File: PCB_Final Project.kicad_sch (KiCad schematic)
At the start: 23 parts, among them J2 Conn_01x02_Pin, J4 Conn_01x02_Socket, K1 SANYOU_SRD_Form_C, Q1 BC547, U1 WeMos_D1_mini, U3 LM393

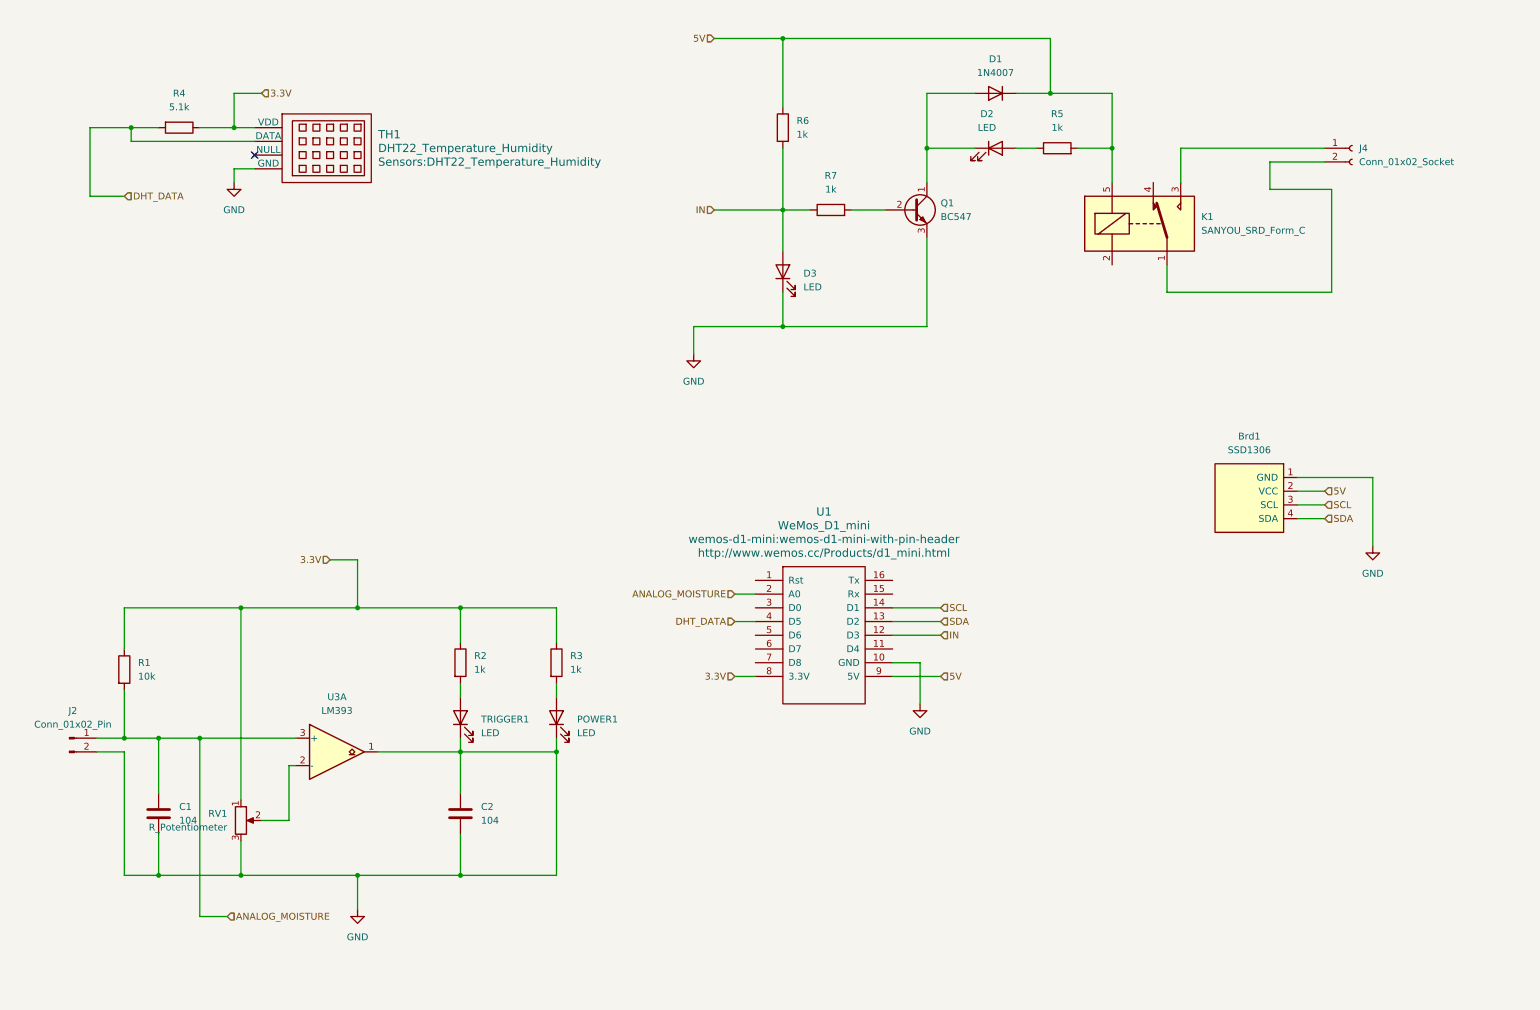
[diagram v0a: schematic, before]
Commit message: update schematic
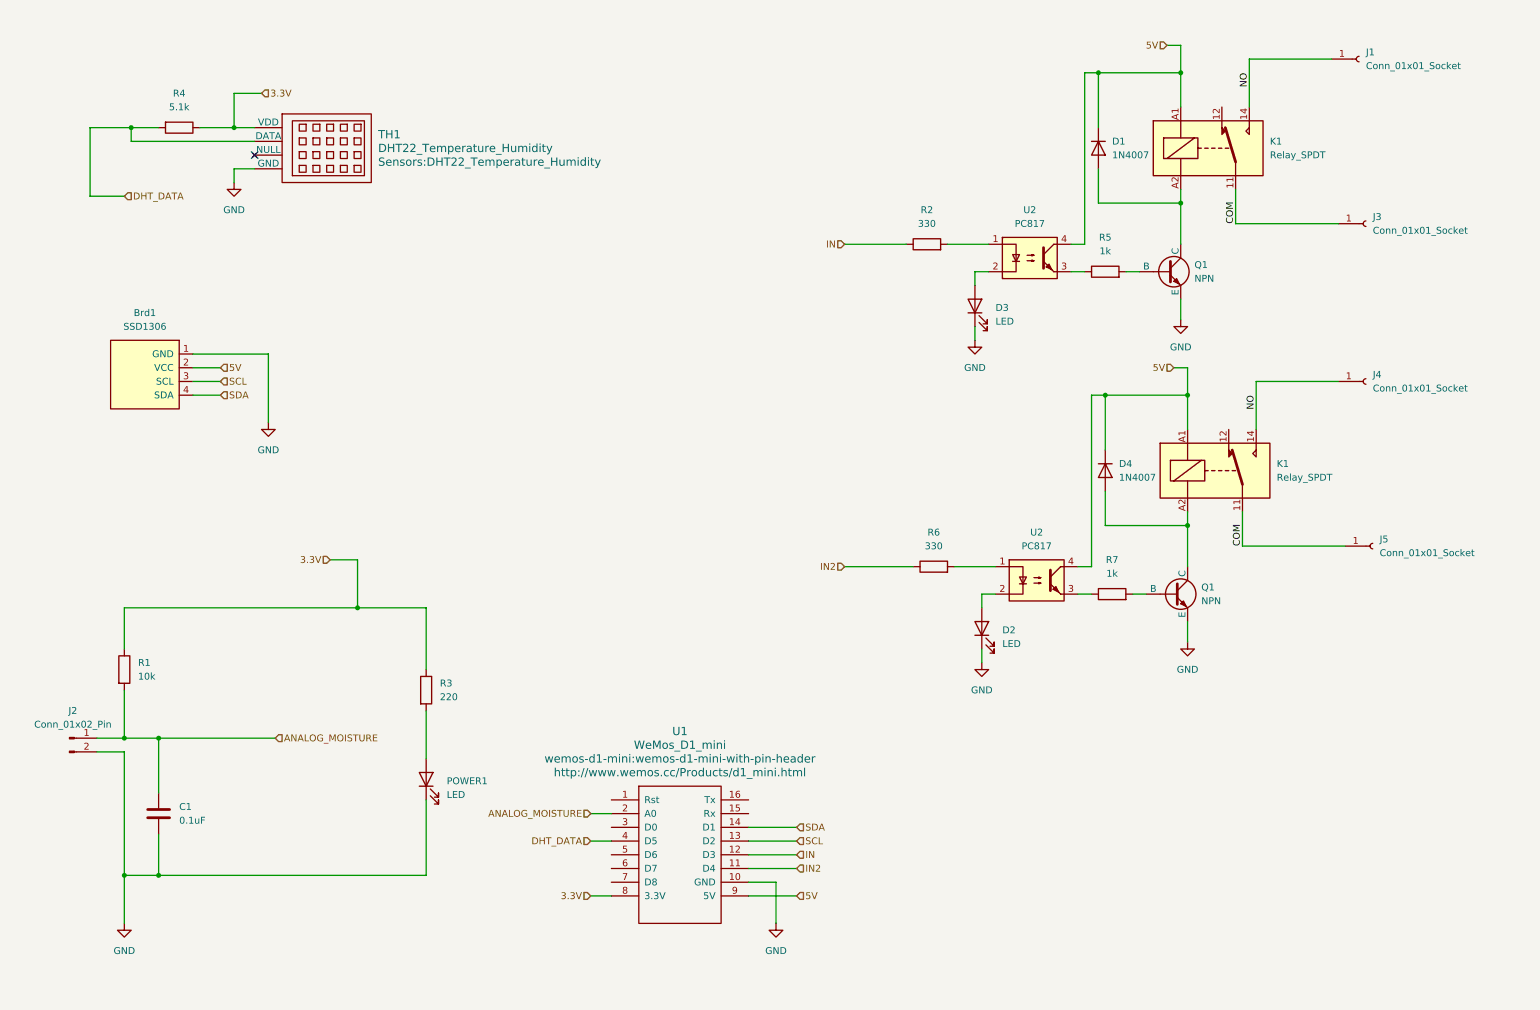
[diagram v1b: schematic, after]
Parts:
- removed C2: 104, Capacitor_SMD:C_0805_2012Metric, symbol Device:C
- removed J4: Conn_01x02_Socket, Connector_PinHeader_2.54mm:PinHeader_1x02_P2.54mm_Vertical, symbol Connector:Conn_01x02_Socket
- removed K1: SANYOU_SRD_Form_C, Relay_SMD:Relay_DPDT_Omron_G6K-2F, symbol Relay:SANYOU_SRD_Form_C
- removed Q1: BC547, Package_TO_SOT_THT:TO-92_Inline, symbol Transistor_BJT:BC547
- removed RV1: R_Potentiometer, Potentiometer_THT:Potentiometer_Piher_PT-15-V02_Vertical_Hole, symbol Device:R_Potentiometer
- removed TRIGGER1: LED, LED_SMD:LED_0805_2012Metric, symbol Device:LED
- removed U3: LM393, Package_DIP:DIP-8_W7.62mm, symbol Comparator:LM393
- added D4: 1N4007, Diode_THT:D_DO-41_SOD81_P10.16mm_Horizontal, symbol Diode:1N4007
- added J1, J3, J4, J5: Conn_01x01_Socket, Connector_PinHeader_2.54mm:PinHeader_1x01_P2.54mm_Vertical, symbol Connector:Conn_01x01_Socket
- added K1 (x2): Relay_SPDT, Relay_THT:Relay_SPDT_Finder_36.11, symbol Relay:Relay_SPDT
- added Q1 (x2): NPN, Package_TO_SOT_SMD:TSOT-23, symbol Simulation_SPICE:NPN
- added U2 (x2): PC817, Package_DIP:DIP-4_W7.62mm_SMDSocket_SmallPads, symbol Isolator:PC817
- C1: value 104 -> 0.1uF
- R2, R6: value 1k -> 330
- R3: value 1k -> 220
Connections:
- net 3.3V: no longer R2.1
- net 5V: now also D4.1 (K), K1.A1, K1.A1, U2.4, U2.4; no longer R5.2, R6.1
- net GND: now also D2.1 (K), Q1.3 (E), Q1.3 (E)
- net IN: now also R2.1; no longer D3.2 (A), R6.2, R7.1
- net SCL: now also U1.13 (D2); no longer U1.14 (D1)
- net SDA: now also U1.14 (D1); no longer U1.13 (D2)
- net at R7.2: now also Q1.2 (B)
- net at R2.2: now also U2.1
- net at D1.2 (A): now also K1.A2, Q1.1 (C); no longer D2.1 (K)
- net at R5.1: now also U2.3; no longer D2.2 (A)
- net IN2: now reaches U1.11 (D4)
- net IN2: now also R6.1
- new net: D4.2 (A), K1.A2, Q1.1 (C)
- new net: R6.2, U2.1
- new net: Q1.2 (B), R5.2
- new net: D3.2 (A), U2.2
- new net: R7.1, U2.3
- new net: D2.2 (A), U2.2
- new net COM: J3.1 (Pin_1), J5.1 (Pin_1), K1.11, K1.11
- new net NO: J1.1 (Pin_1), J4.1 (Pin_1), K1.14, K1.14
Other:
- moved on the sheet: Brd1, POWER1, R3, U1

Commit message: pcb done
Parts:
- removed J1, J3, J4, J5: Conn_01x01_Socket, Connector_PinHeader_2.54mm:PinHeader_1x01_P2.54mm_Vertical, symbol Connector:Conn_01x01_Socket
- added J1, J3: Conn_01x02_Socket, Connector_Wire:SolderWire-2.5sqmm_1x02_P8.8mm_D2.4mm_OD4.4mm, symbol Connector:Conn_01x02_Socket
- D1, D4: footprint Diode_THT:D_DO-41_SOD81_P10.16mm_Horizontal -> Diode_SMD:D_0805_2012Metric
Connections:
- net COM: now also J1.2 (Pin_2), J3.2 (Pin_2)
- net NO: now also J1.1 (Pin_1), J3.1 (Pin_1)
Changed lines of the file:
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@@
+    (stroke (width 0) (type default))
+  )
+  (wire (pts (xy 266.7 99.06) (xy 262.89 99.06))
+    (stroke (width 0) (type default))
+  )
+  (wire (pts (xy 262.89 99.06) (xy 262.89 113.03))
     (stroke (width 0) (type default))
   )
@@
     (stroke (width 0) (type default))
   )
-  (wire (pts (xy 241.3 113.03) (xy 260.35 113.03))
+  (wire (pts (xy 241.3 113.03) (xy 262.89 113.03))
     (stroke (width 0) (type default))
   )
@@
     (stroke (width 0) (type default))
   )
-  (wire (pts (xy 240.03 53.34) (xy 259.08 53.34))
+  (wire (pts (xy 240.03 53.34) (xy 261.62 53.34))
     (stroke (width 0) (type default))
   )
@@
     (stroke (width 0) (type default))
   )
-  (wire (pts (xy 242.57 22.86) (xy 257.81 22.86))
+  (wire (pts (xy 242.57 22.86) (xy 261.62 22.86))
+    (stroke (width 0) (type default))
+  )
+  (wire (pts (xy 261.62 38.1) (xy 264.16 38.1))
     (stroke (width 0) (type default))
   )
@@
     (stroke (width 0) (type default))
   )
-  (wire (pts (xy 243.84 82.55) (xy 259.08 82.55))
+  (wire (pts (xy 243.84 82.55) (xy 262.89 82.55))
     (stroke (width 0) (type default))
   )
@@
     (stroke (width 0) (type default))
   )
+  (wire (pts (xy 262.89 82.55) (xy 262.89 96.52))
+    (stroke (width 0) (type default))
+  )
   (wire (pts (xy 60.96 77.47) (xy 60.96 90.17))
     (stroke (width 0) (type default))
   )
+  (wire (pts (xy 264.16 40.64) (xy 261.62 40.64))
+    (stroke (width 0) (type default))
+  )
   (wire (pts (xy 40.64 148.59) (xy 40.64 158.75))
     (stroke (width 0) (type default))
@@
     (stroke (width 0) (type default))
   )
+  (wire (pts (xy 261.62 22.86) (xy 261.62 38.1))
+    (stroke (width 0) (type default))
+  )
   (wire (pts (xy 40.64 173.99) (xy 90.17 173.99))
     (stroke (width 0) (type default))
@@
   )
   (wire (pts (xy 243.84 91.44) (xy 243.84 82.55))
+    (stroke (width 0) (type default))
+  )
+  (wire (pts (xy 262.89 96.52) (xy 266.7 96.52))
+    (stroke (width 0) (type default))
+  )
+  (wire (pts (xy 261.62 40.64) (xy 261.62 53.34))
     (stroke (width 0) (type default))
   )
@@
       (effects (font (size 1.27 1.27)) (justify left))
     )
-    (property "Footprint" "Diode_THT:D_DO-41_SOD81_P10.16mm_Horizontal" (at 211.455 99.06 0)
+    (property "Footprint" "Diode_SMD:D_0805_2012Metric" (at 211.455 99.06 0)
       (effects (font (size 1.27 1.27)) hide)
     )
@@
         (path "/5c4b6275-3c5c-44a0-af63-482a4c493fbb"
           (reference "D4") (unit 1)
+        )
+      )
+    )
+  )
+  (symbol (lib_id "Connector:Conn_01x02_Socket") (at 271.78 96.52 0) (unit 1)
+    (in_bom yes) (on_board yes) (dnp no) (fields_autoplaced)
+    (property "Reference" "J3" (at 273.05 96.52 0)
+      (effects (font (size 1.27 1.27)) (justify left))
+    )
+    (property "Value" "Conn_01x02_Socket" (at 273.05 99.06 0)
+      (effects (font (size 1.27 1.27)) (justify left))
+    )
+    (property "Footprint" "Connector_Wire:SolderWire-2.5sqmm_1x02_P8.8mm_D2.4mm_OD4.4mm" (at 271.78 96.52 0)
+      (effects (font (size 1.27 1.27)) hide)
+    )
+    (property "Datasheet" "~" (at 271.78 96.52 0)
+      (effects (font (size 1.27 1.27)) hide)
+    )
+    (pin "1")
+    (pin "2")
+    (instances
+      (project "PCB_Final Project"
+        (path "/5c4b6275-3c5c-44a0-af63-482a4c493fbb"
+          (reference "J3") (unit 1)
         )
       )
@@
     )
   )
-  (symbol (lib_id "Connector:Conn_01x01_Socket") (at 264.16 82.55 0) (unit 1)
-    (in_bom yes) (on_board yes) (dnp no) (fields_autoplaced)
-    (property "Reference" "J4" (at 265.43 81.28 0)
-      (effects (font (size 1.27 1.27)) (justify left))
-    )
-    (property "Value" "Conn_01x01_Socket" (at 265.43 83.82 0)
-      (effects (font (size 1.27 1.27)) (justify left))
-    )
-    (property "Footprint" "Connector_PinHeader_2.54mm:PinHeader_1x01_P2.54mm_Vertical" (at 264.16 82.55 0)
-      (effects (font (size 1.27 1.27)) hide)
-    )
-    (property "Datasheet" "~" (at 264.16 82.55 0)
-      (effects (font (size 1.27 1.27)) hide)
-    )
-    (pin "1")
-    (instances
-      (project "PCB_Final Project"
-        (path "/5c4b6275-3c5c-44a0-af63-482a4c493fbb"
-          (reference "J4") (unit 1)
-        )
-      )
-    )
-  )
   (symbol (lib_id "Device:R") (at 34.29 135.89 0) (unit 1)
     (in_bom yes) (on_board yes) (dnp no) (fields_autoplaced)
@@
       (effects (font (size 1.27 1.27)) (justify left))
     )
-    (property "Footprint" "Diode_THT:D_DO-41_SOD81_P10.16mm_Horizontal" (at 210.185 39.37 0)
+    (property "Footprint" "Diode_SMD:D_0805_2012Metric" (at 210.185 39.37 0)
       (effects (font (size 1.27 1.27)) hide)
     )
@@
     )
   )
-  (symbol (lib_id "Connector:Conn_01x01_Socket") (at 264.16 53.34 0) (unit 1)
-    (in_bom yes) (on_board yes) (dnp no) (fields_autoplaced)
-    (property "Reference" "J3" (at 265.43 52.07 0)
-      (effects (font (size 1.27 1.27)) (justify left))
-    )
-    (property "Value" "Conn_01x01_Socket" (at 265.43 54.61 0)
-      (effects (font (size 1.27 1.27)) (justify left))
-    )
-    (property "Footprint" "Connector_PinHeader_2.54mm:PinHeader_1x01_P2.54mm_Vertical" (at 264.16 53.34 0)
-      (effects (font (size 1.27 1.27)) hide)
-    )
-    (property "Datasheet" "~" (at 264.16 53.34 0)
-      (effects (font (size 1.27 1.27)) hide)
-    )
-    (pin "1")
-    (instances
-      (project "PCB_Final Project"
-        (path "/5c4b6275-3c5c-44a0-af63-482a4c493fbb"
-          (reference "J3") (unit 1)
-        )
-      )
-    )
-  )
   (symbol (lib_id "Isolator:PC817") (at 203.2 119.38 0) (unit 1)
     (in_bom yes) (on_board yes) (dnp no) (fields_autoplaced)
@@
         (path "/5c4b6275-3c5c-44a0-af63-482a4c493fbb"
           (reference "D2") (unit 1)
+        )
+      )
+    )
+  )
+  (symbol (lib_id "Connector:Conn_01x02_Socket") (at 269.24 38.1 0) (unit 1)
+    (in_bom yes) (on_board yes) (dnp no) (fields_autoplaced)
+    (property "Reference" "J1" (at 270.51 38.1 0)
+      (effects (font (size 1.27 1.27)) (justify left))
+    )
+    (property "Value" "Conn_01x02_Socket" (at 270.51 40.64 0)
+      (effects (font (size 1.27 1.27)) (justify left))
+    )
+    (property "Footprint" "Connector_Wire:SolderWire-2.5sqmm_1x02_P8.8mm_D2.4mm_OD4.4mm" (at 269.24 38.1 0)
+      (effects (font (size 1.27 1.27)) hide)
+    )
+    (property "Datasheet" "~" (at 269.24 38.1 0)
+      (effects (font (size 1.27 1.27)) hide)
+    )
+    (pin "1")
+    (pin "2")
+    (instances
+      (project "PCB_Final Project"
+        (path "/5c4b6275-3c5c-44a0-af63-482a4c493fbb"
+          (reference "J1") (unit 1)
         )
       )
@@
     )
   )
-  (symbol (lib_id "Connector:Conn_01x01_Socket") (at 265.43 113.03 0) (unit 1)
-    (in_bom yes) (on_board yes) (dnp no) (fields_autoplaced)
-    (property "Reference" "J5" (at 266.7 111.76 0)
-      (effects (font (size 1.27 1.27)) (justify left))
-    )
-    (property "Value" "Conn_01x01_Socket" (at 266.7 114.3 0)
-      (effects (font (size 1.27 1.27)) (justify left))
-    )
-    (property "Footprint" "Connector_PinHeader_2.54mm:PinHeader_1x01_P2.54mm_Vertical" (at 265.43 113.03 0)
-      (effects (font (size 1.27 1.27)) hide)
-    )
-    (property "Datasheet" "~" (at 265.43 113.03 0)
-      (effects (font (size 1.27 1.27)) hide)
-    )
-    (pin "1")
-    (instances
-      (project "PCB_Final Project"
-        (path "/5c4b6275-3c5c-44a0-af63-482a4c493fbb"
-          (reference "J5") (unit 1)
-        )
-      )
-    )
-  )
   (symbol (lib_id "Device:R") (at 182.88 57.15 90) (unit 1)
     (in_bom yes) (on_board yes) (dnp no) (fields_autoplaced)
@@
         )
       )
-    )
-  )
-  (symbol (lib_id "Connector:Conn_01x01_Socket") (at 262.89 22.86 0) (unit 1)
-    (in_bom yes) (on_board yes) (dnp no) (fields_autoplaced)
-    (property "Reference" "J1" (at 264.16 21.59 0)
-      (effects (font (size 1.27 1.27)) (justify left))
-    )
-    (property "Value" "Conn_01x01_Socket" (at 264.16 24.13 0)
-      (effects (font (size 1.27 1.27)) (justify left))
-    )
-    (property "Footprint" "Connector_PinHeader_2.54mm:PinHeader_1x01_P2.54mm_Vertical" (at 262.89 22.86 0)
-      (effects (font (size 1.27 1.27)) hide)
-    )
-    (property "Datasheet" "~" (at 262.89 22.86 0)
-      (effects (font (size 1.27 1.27)) hide)
-    )
-    (pin "1")
-    (instances
-      (project "PCB_Final Project"
-        (path "/5c4b6275-3c5c-44a0-af63-482a4c493fbb"
-          (reference "J1") (unit 1)
-        )
-      )
